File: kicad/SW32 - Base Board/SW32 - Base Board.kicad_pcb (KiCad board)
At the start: 2 copper layers, 198.1 x 99.1 mm, 88 parts, among them J1 AEXP-B, J10 TRG1, J11 TRG2, J12 FRONT_PANEL, J13 DISPLAY, J14 DRV, J15 DRV_PWR, J16 CH_IN, J17 SERIAL, J18 CH1, J19 CH2, J2 AUX1, J20 CH3, J21 CH4, J22 SERIAL_ALT, J23 PWR, J24 BAT, J3 AUX1_ALT, J4 AUX2, J5 AUX2_ALT, J6 AEXP-A, J7 I2C, J8 433TX, J9 PROG, SW1 PWR, U1 PCF8574, U2 ESP32-WROOM-32D, U3 CAT24C256, U4 SP3232, U5 LM2941, U6 TPS5430DDA, U7 NCP1117LP

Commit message: misc. cleanup
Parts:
- J15: value DRV_PWR -> PWR
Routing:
- net GND: vias 40 -> 41
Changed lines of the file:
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@@
       (effects (font (size 1 1) (thickness 0.15)))
     )
-    (fp_text value "DRV_PWR" (at -2.54 3.81 90) (layer "F.SilkS")
+    (fp_text value "PWR" (at -0.000423 10.16 180) (layer "F.SilkS")
+      (effects (font (size 1 1) (thickness 0.15)))
+    )
+    (fp_text user "+12V" (at -3.810423 1.27 unlocked) (layer "F.SilkS")
+      (effects (font (size 1 1) (thickness 0.15)))
+    )
+    (fp_text user "GND" (at -3.175423 6.35 unlocked) (layer "F.SilkS")
       (effects (font (size 1 1) (thickness 0.15)))
     )
@@
       (effects (font (size 1 1) (thickness 0.15)))
     )
-    (fp_line (start -1.33 1.27) (end 1.33 1.27) (layer "F.SilkS") (width 0.12))
+    (fp_line (start -1.33 -1.27) (end 1.33 -1.27) (layer "F.SilkS") (width 0.12))
     (fp_line (start -1.33 8.95) (end 1.33 8.95) (layer "F.SilkS") (width 0.12))
-    (fp_line (start 0 -1.33) (end 1.33 -1.33) (layer "F.SilkS") (width 0.12))
-    (fp_line (start -1.33 1.27) (end -1.33 8.95) (layer "F.SilkS") (width 0.12))
-    (fp_line (start 1.33 -1.33) (end 1.33 0) (layer "F.SilkS") (width 0.12))
-    (fp_line (start 1.33 1.27) (end 1.33 8.95) (layer "F.SilkS") (width 0.12))
+    (fp_line (start -1.33 -1.27) (end -1.33 8.95) (layer "F.SilkS") (width 0.12))
+    (fp_line (start 1.33 -1.27) (end 1.33 8.95) (layer "F.SilkS") (width 0.12))
     (fp_line (start -1.8 -1.8) (end 1.75 -1.8) (layer "F.CrtYd") (width 0.05))
     (fp_line (start -1.8 9.4) (end -1.8 -1.8) (layer "F.CrtYd") (width 0.05))
@@
       (effects (font (size 1 1) (thickness 0.15)))
     )
-    (fp_text value "DRV" (at -2.54 18.288 90) (layer "F.SilkS")
+    (fp_text value "DRV" (at 0 38.1 180) (layer "F.SilkS")
       (effects (font (size 1 1) (thickness 0.15)))
     )
@@
       (effects (font (size 1 1) (thickness 0.15)))
     )
-    (fp_text value "CH_IN" (at 2.286 17.78) (layer "F.SilkS")
+    (fp_text value "CH_IN" (at -2.54 17.78) (layer "F.SilkS")
+      (effects (font (size 1 1) (thickness 0.15)))
+    )
+    (fp_text user "CH4" (at 2.54 33.02 unlocked) (layer "F.SilkS")
+      (effects (font (size 1 1) (thickness 0.15)))
+    )
+    (fp_text user "CH1" (at 2.54 2.54 unlocked) (layer "F.SilkS")
+      (effects (font (size 1 1) (thickness 0.15)))
+    )
+    (fp_text user "CH2" (at 2.54 12.7 unlocked) (layer "F.SilkS")
+      (effects (font (size 1 1) (thickness 0.15)))
+    )
+    (fp_text user "CH3" (at 2.54 22.86 unlocked) (layer "F.SilkS")
       (effects (font (size 1 1) (thickness 0.15)))
     )
@@
       (effects (font (size 1 1) (thickness 0.15)))
     )
-    (fp_line (start 1.33 1.27) (end 1.33 36.89) (layer "F.SilkS") (width 0.12))
-    (fp_line (start -1.33 1.27) (end 1.33 1.27) (layer "F.SilkS") (width 0.12))
-    (fp_line (start 0 -1.33) (end 1.33 -1.33) (layer "F.SilkS") (width 0.12))
-    (fp_line (start -1.33 1.27) (end -1.33 36.89) (layer "F.SilkS") (width 0.12))
-    (fp_line (start 1.33 -1.33) (end 1.33 0) (layer "F.SilkS") (width 0.12))
+    (fp_line (start 1.33 -1.27) (end 1.33 36.89) (layer "F.SilkS") (width 0.12))
+    (fp_line (start -1.33 -1.27) (end 1.33 -1.27) (layer "F.SilkS") (width 0.12))
+    (fp_line (start -1.33 -1.27) (end -1.33 36.89) (layer "F.SilkS") (width 0.12))
     (fp_line (start -1.33 36.89) (end 1.33 36.89) (layer "F.SilkS") (width 0.12))
     (fp_line (start -1.8 37.3) (end -1.8 -1.8) (layer "F.CrtYd") (width 0.05))
@@
   )
   (gr_line locked (start 123.19 167.64) (end 115.57 167.64) (layer "F.SilkS") (width 0.15))
+  (gr_line locked (start 248.92 187.96) (end 248.285 187.96) (layer "F.SilkS") (width 0.15))
   (gr_line locked (start 209.55 200.66) (end 209.55 194.31) (layer "F.SilkS") (width 0.15))
   (gr_line locked (start 186.69 194.31) (end 209.55 194.31) (layer "F.SilkS") (width 0.15))
+  (gr_line locked (start 259.08 188.595) (end 259.08 187.96) (layer "F.SilkS") (width 0.15))
+  (gr_line locked (start 241.24 188.595) (end 241.24 187.96) (layer "F.SilkS") (width 0.15))
+  (gr_line locked (start 269.24 187.96) (end 268.605 187.96) (layer "F.SilkS") (width 0.15))
   (gr_line locked (start 186.69 194.31) (end 186.69 134.62) (layer "F.SilkS") (width 0.15))
-  (gr_line (start 311.15 200.66) (end 311.15 138.43) (layer "F.SilkS") (width 0.15))
+  (gr_line locked (start 271.78 187.96) (end 272.415 187.96) (layer "F.SilkS") (width 0.15))
+  (gr_line locked (start 311.15 200.66) (end 311.15 138.43) (layer "F.SilkS") (width 0.15))
+  (gr_line locked (start 271.78 188.595) (end 271.78 187.96) (layer "F.SilkS") (width 0.15))
   (gr_line locked (start 311.15 200.66) (end 209.55 200.66) (layer "F.SilkS") (width 0.15))
   (gr_line locked (start 311.15 134.62) (end 311.15 135.89) (layer "F.SilkS") (width 0.15))
   (gr_line locked (start 185.42 200.66) (end 185.42 157.48) (layer "F.SilkS") (width 0.15))
+  (gr_line locked (start 241.24 187.96) (end 241.935 187.96) (layer "F.SilkS") (width 0.15))
   (gr_line locked (start 115.57 167.64) (end 115.57 200.66) (layer "F.SilkS") (width 0.15))
+  (gr_line locked (start 248.92 188.595) (end 248.92 187.96) (layer "F.SilkS") (width 0.15))
+  (gr_line locked (start 269.24 188.595) (end 269.24 187.96) (layer "F.SilkS") (width 0.15))
   (gr_line locked (start 311.15 134.62) (end 186.69 134.62) (layer "F.SilkS") (width 0.15))
+  (gr_line locked (start 279.4 188.595) (end 279.4 187.96) (layer "F.SilkS") (width 0.15))
+  (gr_line locked (start 279.4 187.96) (end 278.765 187.96) (layer "F.SilkS") (width 0.15))
   (gr_line locked (start 115.57 200.66) (end 185.42 200.66) (layer "F.SilkS") (width 0.15))
+  (gr_line locked (start 304.165 148.59) (end 303.53 148.59) (layer "F.SilkS") (width 0.15))
+  (gr_line locked (start 251.46 187.96) (end 251.46 188.595) (layer "F.SilkS") (width 0.15))
+  (gr_line locked (start 261.62 188.595) (end 261.62 187.96) (layer "F.SilkS") (width 0.15))
+  (gr_line locked (start 304.165 143.51) (end 303.53 143.51) (layer "F.SilkS") (width 0.15))
+  (gr_line locked (start 251.46 187.96) (end 252.095 187.96) (layer "F.SilkS") (width 0.15))
+  (gr_line locked (start 303.53 143.51) (end 303.53 144.145) (layer "F.SilkS") (width 0.15))
+  (gr_line locked (start 303.53 153.67) (end 303.53 153.035) (layer "F.SilkS") (width 0.15))
   (gr_line locked (start 185.42 157.48) (end 123.19 157.48) (layer "F.SilkS") (width 0.15))
+  (gr_line locked (start 304.165 153.67) (end 303.53 153.67) (layer "F.SilkS") (width 0.15))
+  (gr_line locked (start 261.62 187.96) (end 262.255 187.96) (layer "F.SilkS") (width 0.15))
+  (gr_line locked (start 259.08 187.96) (end 258.445 187.96) (layer "F.SilkS") (width 0.15))
   (gr_line locked (start 123.19 157.48) (end 123.19 167.64) (layer "F.SilkS") (width 0.15))
   (gr_rect locked (start 124.36 128.27) (end 149.86 153.67) (layer "Cmts.User") (width 0.15) (fill none))
@@
   (via locked (at 139.7 171.842071) (size 0.8) (drill 0.4) (layers "F.Cu" "B.Cu") (free) (net 5))
   (via locked (at 210.82 163.470608) (size 0.8) (drill 0.4) (layers "F.Cu" "B.Cu") (free) (net 5))
+  (via locked (at 129.54 147.32) (size 0.8) (drill 0.4) (layers "F.Cu" "B.Cu") (free) (net 5))
   (via locked (at 175.82 163.83) (size 0.8) (drill 0.4) (layers "F.Cu" "B.Cu") (free) (net 5))
   (via locked (at 130.175 137.795) (size 0.8) (drill 0.4) (layers "F.Cu" "B.Cu") (free) (net 5))
@@
   (segment locked (start 135.9 129.54) (end 135.9 131.600512) (width 0.5) (layer "B.Cu") (net 6))
   (segment locked (start 160.7725 139.705) (end 163.855736 142.788236) (width 0.5) (layer "B.Cu") (net 6))
-  (segment (start 208.114361 193.971085) (end 208.114361 188.291599) (width 0.6) (layer "F.Cu") (net 7))
+  (segment locked (start 208.114361 193.971085) (end 208.114361 188.291599) (width 0.6) (layer "F.Cu") (net 7))
   (segment locked (start 181.135752 135.094248) (end 205.017185 135.094248) (width 1) (layer "F.Cu") (net 7))
   (segment locked (start 201.93 149.86) (end 199.39 149.86) (width 0.6) (layer "F.Cu") (net 7))
@@
   (segment locked (start 220.079898 159.33711) (end 218.2 161.217008) (width 1) (layer "F.Cu") (net 7))
   (segment locked (start 212.09 170.18) (end 207.01 165.1) (width 0.6) (layer "F.Cu") (net 7))
-  (segment (start 208.114361 188.291599) (end 217.17 179.23596) (width 0.6) (layer "F.Cu") (net 7))
+  (segment locked (start 208.114361 188.291599) (end 217.17 179.23596) (width 0.6) (layer "F.Cu") (net 7))
   (segment locked (start 272.796 156.083) (end 272.796 167.229814) (width 0.3) (layer "F.Cu") (net 7))
   (segment locked (start 217.17 170.18) (end 212.09 170.18) (width 0.6) (layer "F.Cu") (net 7))
   (segment locked (start 220.079898 150.156961) (end 220.079898 159.33711) (width 1) (layer "F.Cu") (net 7))
-  (segment (start 204.47 197.615446) (end 208.114361 193.971085) (width 0.6) (layer "F.Cu") (net 7))
+  (segment locked (start 204.47 197.615446) (end 208.114361 193.971085) (width 0.6) (layer "F.Cu") (net 7))
   (segment locked (start 207.01 165.1) (end 207.01 154.94) (width 0.6) (layer "F.Cu") (net 7))
-  (segment (start 217.17 179.23596) (end 217.17 170.18) (width 0.6) (layer "F.Cu") (net 7))
+  (segment locked (start 217.17 179.23596) (end 217.17 170.18) (width 0.6) (layer "F.Cu") (net 7))
   (segment locked (start 179.07 137.16) (end 181.135752 135.094248) (width 1) (layer "F.Cu") (net 7))
   (segment locked (start 207.01 154.94) (end 201.93 149.86) (width 0.6) (layer "F.Cu") (net 7))

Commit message: add cap
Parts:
- added C3: 100nF, Capacitor_SMD:C_0603_1608Metric, F.Cu at (123.8, 154.1)
- moved C2 2.45 mm to (123.9, 156.6)
- renumbered C9 to C10, C10 to C11, C11 to C12, C12 to C13, C13 to C14, C14 to C15, C15 to C16, C16 to C17, C3 to C4, C4 to C5, C5 to C6, C6 to C7, C7 to C8, C8 to C9
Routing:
- net +3.3V: track 389.0 -> 392.0 mm

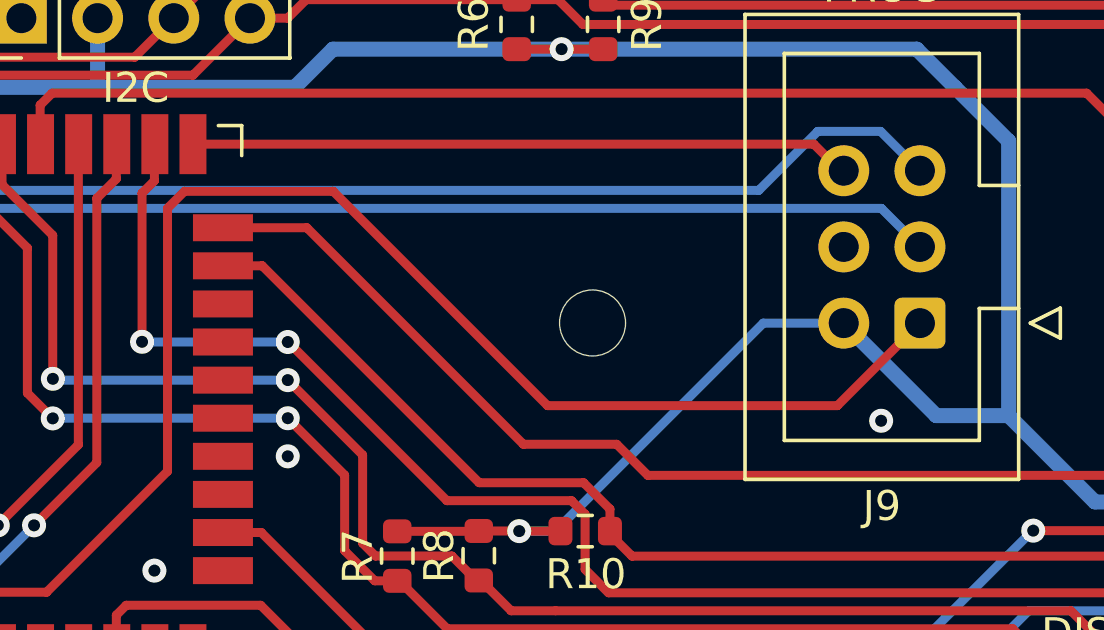
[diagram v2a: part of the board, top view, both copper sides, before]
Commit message: fix auto program
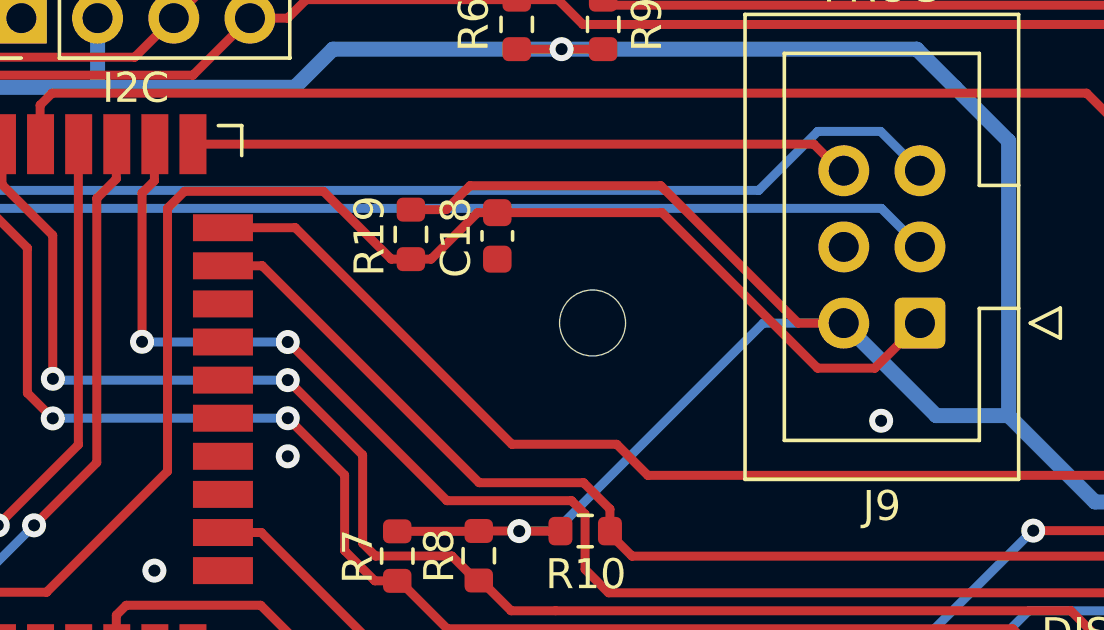
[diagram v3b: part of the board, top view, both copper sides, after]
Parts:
- added C18: 100nF, Capacitor_SMD:C_0603_1608Metric, F.Cu at (149.2, 136.8)
- added R19: 10K, Resistor_SMD:R_0603_1608Metric, F.Cu at (146.3, 136.7)
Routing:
- net +3.3V: track 392.0 -> 408.7 mm
